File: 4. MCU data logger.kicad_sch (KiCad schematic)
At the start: 0 parts

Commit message: Symbols have been added
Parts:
- added BT1: Battery, symbol Device:Battery
- added C1, C3, C4, C5, C6: C, symbol Device:C
- added C2: C_Polarized, symbol Device:C_Polarized
- added D1, D2: LED, symbol Device:LED
- added H1, H2, H3, H4: MountingHole, symbol Mechanical:MountingHole
- added R1, R2, R3, R4, R5, R6, R7: R, symbol Device:R
- added U1, U2: 24LC1025, symbol Memory_EEPROM:24LC1025
- added U3: DS1307_, digikey-footprints:DIP-8_W7.62mm, symbol dk_Clock-Timing-Real-Time-Clocks:DS1307_
- added U4: ATMEGA328P-AU, ATMEGA328P-AU:QFP80P900X900X120-32N, symbol ATMEGA328P-AU:ATMEGA328P-AU
- added Y1, Y2: Crystal, symbol Device:Crystal
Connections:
- new net: U4.21 (GND), U4.3 (GND), U4.5 (GND)
- new net: U4.4 (VCC), U4.6 (VCC)
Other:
- added sheet Connectors (connectors.kicad_sch)

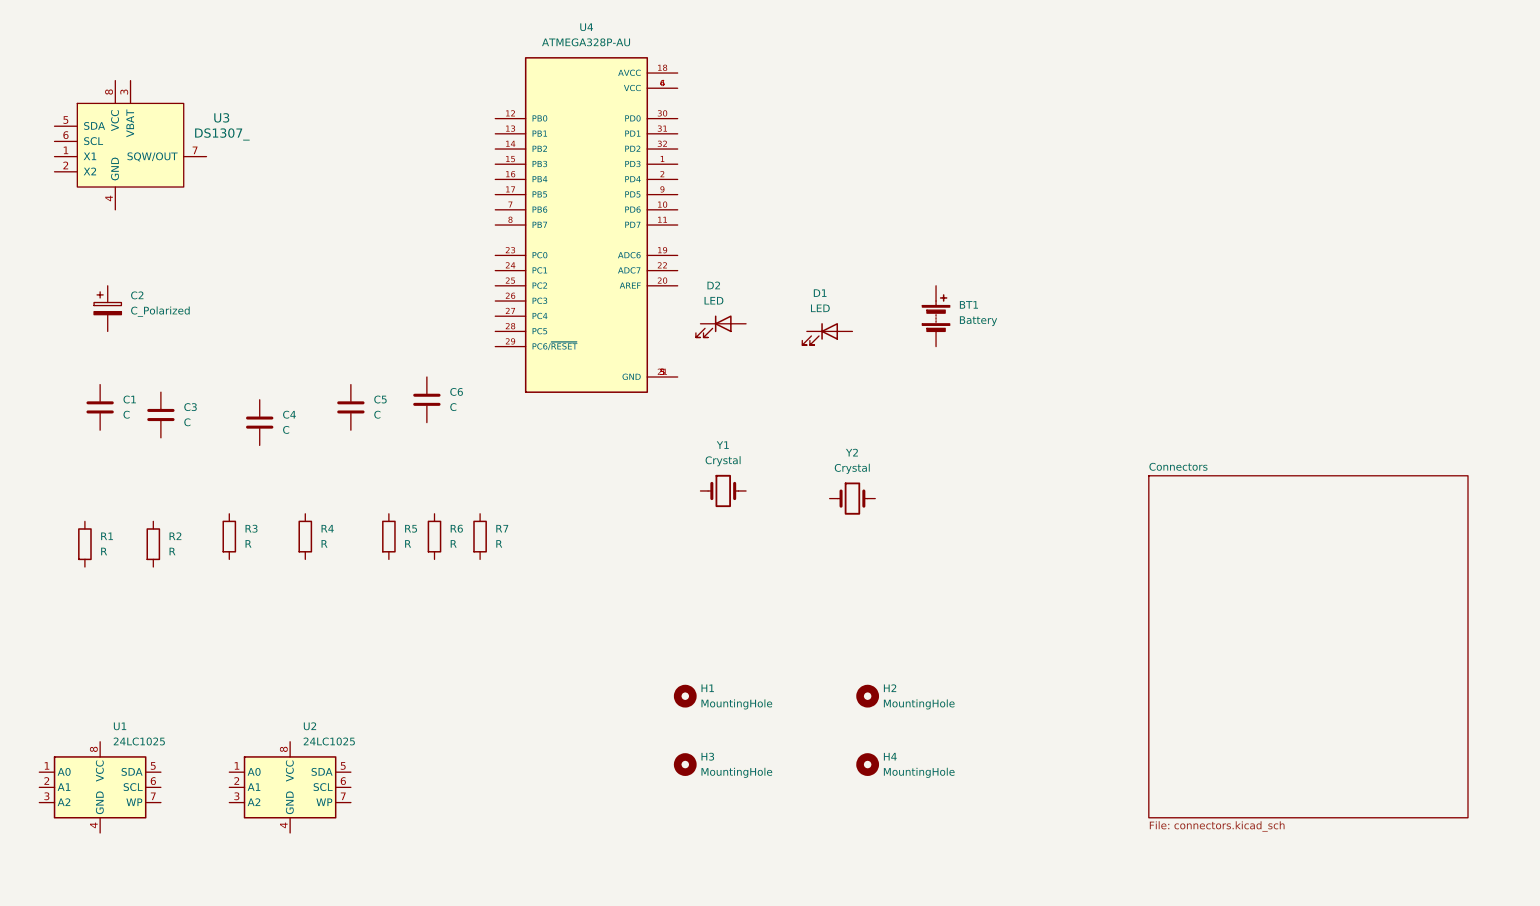
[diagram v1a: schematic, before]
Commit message: Symbols values have been added
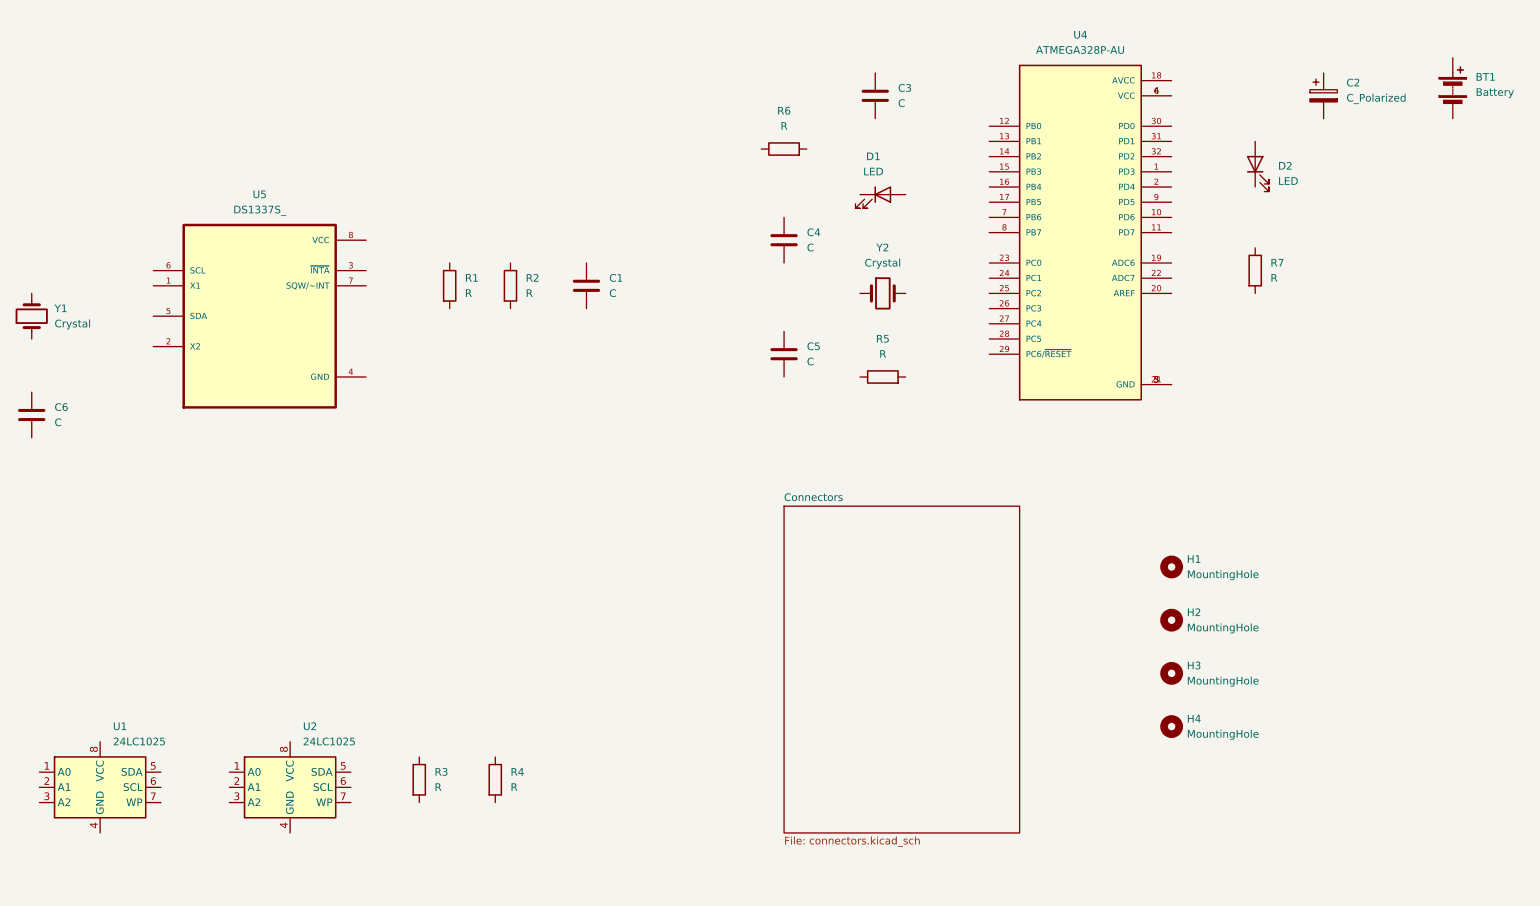
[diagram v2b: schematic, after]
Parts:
- removed U3: DS1307_, digikey-footprints:DIP-8_W7.62mm, symbol dk_Clock-Timing-Real-Time-Clocks:DS1307_
- added U5: DS1337S_, DS1337S_:SOIC127P600X175-8N, symbol DS1337S_:DS1337S_
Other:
- moved on the sheet: BT1, C1, C2, C3, C4, C5, C6, D1, D2, H1, H2, H3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

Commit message: Footprints associated
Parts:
- removed C6: C, symbol Device:C
- BT1: footprint (none) -> Connector_PinHeader_2.54mm:PinHeader_1x02_P2.54mm_Vertical
- C1, C3: value C -> 0.1uF; footprint (none) -> Capacitor_SMD:C_0805_2012Metric
- C2: value C_Polarized -> 100 nF; footprint (none) -> Capacitor_SMD:C_0805_2012Metric
- C4, C5: value C -> 22pF; footprint (none) -> Capacitor_SMD:C_0805_2012Metric
- D1, D2: footprint (none) -> LED_SMD:LED_0805_2012Metric
- H1, H2, H3, H4: footprint (none) -> MountingHole:MountingHole_2.1mm
- R1, R2, R5: value R -> 10K; footprint (none) -> Resistor_SMD:R_0805_2012Metric
- R3, R4: value R -> 4.7K; footprint (none) -> Resistor_SMD:R_0805_2012Metric
- R6, R7: value R -> 330; footprint (none) -> Resistor_SMD:R_0805_2012Metric
- U1, U2: footprint (none) -> Package_SO:SOIC-8_5.3x5.3mm_P1.27mm
- Y1: value Crystal -> 32.768 KHz; footprint (none) -> Crystal:Crystal_SMD_5032-2Pin_5.0x3.2mm_HandSoldering
- Y2: value Crystal -> 16 MHz; footprint (none) -> Crystal:Crystal_SMD_5032-2Pin_5.0x3.2mm_HandSoldering

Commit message: wiring has been done
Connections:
- net GND: now reaches C5.1
- net GND: now also BT1.2 (-), C1.2, C2.2, C3.1, C4.1, R6.1, R7.2, U1.4 (GND), U1.7 (WP), U2.2 (A1), U2.4 (GND), U2.7 (WP), U4.21 (GND), U4.3 (GND), U4.5 (GND), U5.4 (GND)
- net at C5.2: now also U4.8 (PB7), Y2.1
- net VCC: now reaches R5.1
- net VCC: now also C1.1, R1.1, R2.1, R3.1, R4.1, U1.1 (A0), U1.2 (A1), U1.3 (A2), U1.8 (VCC), U2.1 (A0), U2.3 (A2), U2.8 (VCC), U5.8 (VCC)
- net RESET: now reaches R5.2
- net RESET: now also U4.29 (PC6/~{RESET})
- net at BT1.1 (+): now also C2.1, D2.2 (A), U4.18 (AVCC), U4.4 (VCC)
- net at R7.1: now also D2.1 (K)
- net at C4.2: now also U4.7 (PB6), Y2.2
- net at R1.2: now also U5.3 (~{INTA})
- net at U5.1 (X1): now also Y1.2
- net at U5.2 (X2): now also Y1.1
- net SDA: now reaches U5.5 (SDA)
- net SDA: now also R4.2, U1.5 (SDA), U2.5 (SDA), U4.27 (PC4)
- net SCK: now reaches U5.6 (SCL)
- net SCK: now also D1.2 (A), R3.2, U1.6 (SCL), U2.6 (SCL), U4.17 (PB5), U4.28 (PC5)
- net at U5.7 (SQW/~INT): now also R2.2
- net at C3.2: now also U4.20 (AREF)
- net at R6.2: now also D1.1 (K)
- net D3: now reaches U4.1 (PD3)
- net D6: now reaches U4.10 (PD6)
- net D7: now reaches U4.11 (PD7)
- net D8: now reaches U4.12 (PB0)
- net MOSI: now reaches U4.15 (PB3)
- net MISO: now reaches U4.16 (PB4)
- net D4: now reaches U4.2 (PD4)
- net RX: now reaches U4.30 (PD0)
- net TX: now reaches U4.31 (PD1)
- net D2: now reaches U4.32 (PD2)
- net at U4.6 (VCC): no longer U4.4 (VCC)
- net D5: now reaches U4.9 (PD5)
- no-connect marks 0 -> 9
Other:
- sheet Connectors ports: added D2, D3, D4, D5, D6, D7, D8, GND, MISO, MOSI, RESET, RX, SCK, SDA, TX, VCC; removed none
- moved on the sheet: BT1, C1, C2, C3, C4, C5, D1, D2, R1, R2, R5, R7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
